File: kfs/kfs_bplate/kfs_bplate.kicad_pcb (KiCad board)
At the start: 2 copper layers, 256 x 90.6 mm, 10 parts

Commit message: Slight mods to kfs.
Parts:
- added H1: MountingHole, MountingHole:MountingHole_4mm, F.Cu at (135.0, 34.0)
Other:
- board size 256 x 90.6 mm -> 256 x 94.5 mm
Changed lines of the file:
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@@
     (pad "1" thru_hole circle (at 0 0) (size 3.5 3.5) (drill 2.2) (layers "*.Cu" "*.Mask"))
+  )
+  (footprint "MountingHole:MountingHole_4mm" (layer "F.Cu")
+    (at 135 34)
+    (descr "Mounting Hole 4mm, no annular")
+    (tags "mounting hole 4mm no annular")
+    (property "Sheetfile" "kfs_bplate.kicad_sch")
+    (property "Sheetname" "")
+    (property "ki_description" "Mounting Hole without connection")
+    (property "ki_keywords" "mounting hole")
+    (attr exclude_from_pos_files)
+    (fp_text reference "H1" (at 0 -5) (layer "F.SilkS") hide
+        (effects (font (size 1 1) (thickness 0.15)))
+    )
+    (fp_text value "MountingHole" (at 0 5) (layer "F.Fab")
+        (effects (font (size 1 1) (thickness 0.15)))
+    )
+    (fp_text user "${REFERENCE}" (at 0 0) (layer "F.Fab")
+        (effects (font (size 1 1) (thickness 0.15)))
+    )
+    (fp_circle (center 0 0) (end 4 0)
+      (stroke (width 0.15) (type solid)) (fill none) (layer "Cmts.User"))
+    (fp_circle (center 0 0) (end 4.25 0)
+      (stroke (width 0.05) (type solid)) (fill none) (layer "F.CrtYd"))
+    (pad "" np_thru_hole circle (at 0 0) (size 4 4) (drill 4) (layers "*.Cu" "*.Mask"))
   )
   (footprint "MountingHole:MountingHole_2.2mm_M2_ISO7380_Pad" (layer "F.Cu")
@@
     (pad "1" thru_hole circle (at 0 0) (size 3.5 3.5) (drill 2.2) (layers "*.Cu" "*.Mask"))
   )
-  (gr_line (start 268 21.94) (end 20 21.94)
+  (gr_line (start 268 18) (end 20 18)
     (stroke (width 0.1) (type default)) (layer "Edge.Cuts"))
-  (gr_arc (start 16 25.94) (mid 17.171573 23.111573) (end 20 21.94)
+  (gr_arc (start 16 22) (mid 17.171573 19.171573) (end 20 18)
     (stroke (width 0.1) (type default)) (layer "Edge.Cuts"))
   (gr_arc (start 20 112.5) (mid 17.171573 111.328427) (end 16 108.5)
     (stroke (width 0.1) (type default)) (layer "Edge.Cuts"))
-  (gr_arc (start 268 21.94) (mid 270.828427 23.111573) (end 272 25.94)
-    (stroke (width 0.1) (type default)) (layer "Edge.Cuts"))
   (gr_arc (start 272 108.5) (mid 270.828427 111.328427) (end 268 112.5)
     (stroke (width 0.1) (type default)) (layer "Edge.Cuts"))
-  (gr_line (start 16 25.94) (end 16 108.5)
+  (gr_line (start 16 22) (end 16 108.5)
     (stroke (width 0.1) (type default)) (layer "Edge.Cuts"))
   (gr_line (start 20 112.5) (end 268 112.5)
     (stroke (width 0.1) (type default)) (layer "Edge.Cuts"))
-  (gr_line (start 272 108.5) (end 272 25.94)
+  (gr_line (start 272 108.5) (end 272 22)
+    (stroke (width 0.1) (type default)) (layer "Edge.Cuts"))
+  (gr_arc (start 268 18) (mid 270.828427 19.171573) (end 272 22)
     (stroke (width 0.1) (type default)) (layer "Edge.Cuts"))
 )

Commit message: Moved some mounting holes on the kfs.
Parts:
- moved H0 23.2 mm to (148.0, 24.0)
- moved H4 23.2 mm to (122.0, 24.0)
- moved H3 17.0 mm to (216.0, 59.5)
- moved H7 14.1 mm to (22.0, 24.0)
- moved H9 14.1 mm to (266.0, 24.0)
- moved H10 4.53 mm to (266.0, 106.5)
- moved H8 4.53 mm to (22.0, 106.5)
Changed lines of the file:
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@@
   (net 0 "")
   (footprint "MountingHole:MountingHole_2.2mm_M2_ISO7380_Pad" (layer "F.Cu")
-    (at 162 42.5)
+    (at 148 24)
     (descr "Mounting Hole 2.2mm, M2, ISO7380")
     (tags "mounting hole 2.2mm m2 iso7380")
@@
   )
   (footprint "MountingHole:MountingHole_2.2mm_M2_ISO7380_Pad" (layer "F.Cu")
-    (at 265.5 102)
+    (at 266 106.5)
     (descr "Mounting Hole 2.2mm, M2, ISO7380")
     (tags "mounting hole 2.2mm m2 iso7380")
@@
   )
   (footprint "MountingHole:MountingHole_2.2mm_M2_ISO7380_Pad" (layer "F.Cu")
-    (at 22.5 102)
+    (at 22 106.5)
     (descr "Mounting Hole 2.2mm, M2, ISO7380")
     (tags "mounting hole 2.2mm m2 iso7380")
@@
   )
   (footprint "MountingHole:MountingHole_2.2mm_M2_ISO7380_Pad" (layer "F.Cu")
-    (at 36 25.5)
+    (at 22 24)
     (descr "Mounting Hole 2.2mm, M2, ISO7380")
     (tags "mounting hole 2.2mm m2 iso7380")
@@
   )
   (footprint "MountingHole:MountingHole_2.2mm_M2_ISO7380_Pad" (layer "F.Cu")
-    (at 108 42.5)
+    (at 122 24)
     (descr "Mounting Hole 2.2mm, M2, ISO7380")
     (tags "mounting hole 2.2mm m2 iso7380")
@@
   )
   (footprint "MountingHole:MountingHole_2.2mm_M2_ISO7380_Pad" (layer "F.Cu")
-    (at 216 76.5)
+    (at 216 59.5)
     (descr "Mounting Hole 2.2mm, M2, ISO7380")
     (tags "mounting hole 2.2mm m2 iso7380")
@@
   )
   (footprint "MountingHole:MountingHole_2.2mm_M2_ISO7380_Pad" (layer "F.Cu")
-    (at 252 25.5)
-    (descr "Mounting Hole 2.2mm, M2, ISO7380")
-    (tags "mounting hole 2.2mm m2 iso7380")
+    (at 266 24)
+    (descr "Mounting Hole 2.2mm, M2, ISO7380")
+    (tags "mounting hole 2.2mm m2 iso7380")

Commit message: Switched to staggered kfs layout.
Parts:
- H1: footprint MountingHole:MountingHole_4mm -> MountingHole:MountingHole_8.4mm_M8
- moved H3 200.3 mm to (16.5, 41.5)
- moved H8 196.2 mm to (216.0, 77.0)
- moved H5 184.1 mm to (289.5, 124.5)
- moved H10 150.7 mm to (130.0, 41.5)
- moved H2 137.7 mm to (289.5, 41.5)
- moved H4 114.1 mm to (176.0, 124.5)
- moved H9 109.4 mm to (158.0, 41.5)
- moved H0 106.8 mm to (112.0, 124.5)
- moved H6 85.5 mm to (16.5, 124.5)
- moved H7 72.9 mm to (72.0, 77.0)
- moved H1 19.2 mm to (144.0, 51.0)
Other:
- board size 256 x 94.5 mm -> 283 x 93 mm
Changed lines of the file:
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@@
   (net 0 "")
   (footprint "MountingHole:MountingHole_2.2mm_M2_ISO7380_Pad" (layer "F.Cu")
-    (at 148 24)
+    (at 112 124.5)
     (descr "Mounting Hole 2.2mm, M2, ISO7380")
     (tags "mounting hole 2.2mm m2 iso7380")
@@
   )
   (footprint "MountingHole:MountingHole_2.2mm_M2_ISO7380_Pad" (layer "F.Cu")
-    (at 266 106.5)
+    (at 130 41.5)
     (descr "Mounting Hole 2.2mm, M2, ISO7380")
     (tags "mounting hole 2.2mm m2 iso7380")
@@
   )
   (footprint "MountingHole:MountingHole_2.2mm_M2_ISO7380_Pad" (layer "F.Cu")
-    (at 162 93.5)
+    (at 289.5 41.5)
     (descr "Mounting Hole 2.2mm, M2, ISO7380")
     (tags "mounting hole 2.2mm m2 iso7380")
@@
     (pad "1" thru_hole circle (at 0 0) (size 3.5 3.5) (drill 2.2) (layers "*.Cu" "*.Mask"))
   )
-  (footprint "MountingHole:MountingHole_2.2mm_M2_ISO7380_Pad" (layer "F.Cu")
-    (at 72 59.5)
+  (footprint "MountingHole:MountingHole_8.4mm_M8" (layer "F.Cu")
+    (at 144 51)
+    (descr "Mounting Hole 8.4mm, no annular, M8")
+    (tags "mounting hole 8.4mm no annular m8")
+    (property "Sheetfile" "kfs_bplate.kicad_sch")
+    (property "Sheetname" "")
+    (property "ki_description" "Mounting Hole without connection")
+    (property "ki_keywords" "mounting hole")
+    (attr exclude_from_pos_files)
+    (fp_text reference "H1" (at 0 -9.4) (layer "F.SilkS") hide
+        (effects (font (size 1 1) (thickness 0.15)))
+    )
+    (fp_text value "MountingHole" (at 0 9.4) (layer "F.Fab")
+        (effects (font (size 1 1) (thickness 0.15)))
+    )
+    (fp_text user "${REFERENCE}" (at 0 0) (layer "F.Fab")
+        (effects (font (size 1 1) (thickness 0.15)))
+    )
+    (fp_circle (center 0 0) (end 8.4 0)
+      (stroke (width 0.15) (type solid)) (fill none) (layer "Cmts.User"))
+    (fp_circle (center 0 0) (end 8.65 0)
+      (stroke (width 0.05) (type solid)) (fill none) (layer "F.CrtYd"))
+    (pad "" np_thru_hole circle (at 0 0) (size 8.4 8.4) (drill 8.4) (layers "*.Cu" "*.Mask"))
+  )
+  (footprint "MountingHole:MountingHole_2.2mm_M2_ISO7380_Pad" (layer "F.Cu")
+    (at 16.5 124.5)
     (descr "Mounting Hole 2.2mm, M2, ISO7380")
     (tags "mounting hole 2.2mm m2 iso7380")
@@
   )
   (footprint "MountingHole:MountingHole_2.2mm_M2_ISO7380_Pad" (layer "F.Cu")
-    (at 22 106.5)
+    (at 216 77)
     (descr "Mounting Hole 2.2mm, M2, ISO7380")
     (tags "mounting hole 2.2mm m2 iso7380")
@@
   )
   (footprint "MountingHole:MountingHole_2.2mm_M2_ISO7380_Pad" (layer "F.Cu")
-    (at 22 24)
+    (at 72 77)
     (descr "Mounting Hole 2.2mm, M2, ISO7380")
     (tags "mounting hole 2.2mm m2 iso7380")
@@
   )
   (footprint "MountingHole:MountingHole_2.2mm_M2_ISO7380_Pad" (layer "F.Cu")
-    (at 122 24)
+    (at 176 124.5)
     (descr "Mounting Hole 2.2mm, M2, ISO7380")
     (tags "mounting hole 2.2mm m2 iso7380")
@@
   )
   (footprint "MountingHole:MountingHole_2.2mm_M2_ISO7380_Pad" (layer "F.Cu")
-    (at 108 93.5)
+    (at 289.5 124.5)
     (descr "Mounting Hole 2.2mm, M2, ISO7380")
     (tags "mounting hole 2.2mm m2 iso7380")
@@
   )
   (footprint "MountingHole:MountingHole_2.2mm_M2_ISO7380_Pad" (layer "F.Cu")
-    (at 216 59.5)
+    (at 16.5 41.5)
     (descr "Mounting Hole 2.2mm, M2, ISO7380")
     (tags "mounting hole 2.2mm m2 iso7380")
@@
     (pad "1" thru_hole circle (at 0 0) (size 3.5 3.5) (drill 2.2) (layers "*.Cu" "*.Mask"))
   )
-  (footprint "MountingHole:MountingHole_4mm" (layer "F.Cu")
-    (at 135 34)
-    (descr "Mounting Hole 4mm, no annular")
-    (tags "mounting hole 4mm no annular")
-    (property "Sheetfile" "kfs_bplate.kicad_sch")
-    (property "Sheetname" "")
-    (property "ki_description" "Mounting Hole without connection")
-    (property "ki_keywords" "mounting hole")
-    (attr exclude_from_pos_files)
-    (fp_text reference "H1" (at 0 -5) (layer "F.SilkS") hide
-        (effects (font (size 1 1) (thickness 0.15)))
-    )
-    (fp_text value "MountingHole" (at 0 5) (layer "F.Fab")
-        (effects (font (size 1 1) (thickness 0.15)))
-    )
-    (fp_text user "${REFERENCE}" (at 0 0) (layer "F.Fab")
-        (effects (font (size 1 1) (thickness 0.15)))
-    )
-    (fp_circle (center 0 0) (end 4 0)
-      (stroke (width 0.15) (type solid)) (fill none) (layer "Cmts.User"))
-    (fp_circle (center 0 0) (end 4.25 0)
-      (stroke (width 0.05) (type solid)) (fill none) (layer "F.CrtYd"))
-    (pad "" np_thru_hole circle (at 0 0) (size 4 4) (drill 4) (layers "*.Cu" "*.Mask"))
-  )
-  (footprint "MountingHole:MountingHole_2.2mm_M2_ISO7380_Pad" (layer "F.Cu")
-    (at 266 24)
+  (footprint "MountingHole:MountingHole_2.2mm_M2_ISO7380_Pad" (layer "F.Cu")
+    (at 158 41.5)
     (descr "Mounting Hole 2.2mm, M2, ISO7380")
     (tags "mounting hole 2.2mm m2 iso7380")
@@
     (pad "1" thru_hole circle (at 0 0) (size 3.5 3.5) (drill 2.2) (layers "*.Cu" "*.Mask"))
   )
-  (gr_line (start 268 18) (end 20 18)
-    (stroke (width 0.1) (type default)) (layer "Edge.Cuts"))
-  (gr_arc (start 16 22) (mid 17.171573 19.171573) (end 20 18)
-    (stroke (width 0.1) (type default)) (layer "Edge.Cuts"))
-  (gr_arc (start 20 112.5) (mid 17.171573 111.328427) (end 16 108.5)
-    (stroke (width 0.1) (type default)) (layer "Edge.Cuts"))
-  (gr_arc (start 272 108.5) (mid 270.828427 111.328427) (end 268 112.5)
-    (stroke (width 0.1) (type default)) (layer "Edge.Cuts"))
-  (gr_line (start 16 22) (end 16 108.5)
-    (stroke (width 0.1) (type default)) (layer "Edge.Cuts"))
-  (gr_line (start 20 112.5) (end 268 112.5)
-    (stroke (width 0.1) (type default)) (layer "Edge.Cuts"))
-  (gr_line (start 272 108.5) (end 272 22)
-    (stroke (width 0.1) (type default)) (layer "Edge.Cuts"))
-  (gr_arc (start 268 18) (mid 270.828427 19.171573) (end 272 22)
+  (gr_arc (start 16.5 129.5) (mid 12.964466 128.035534) (end 11.5 124.5)
+    (stroke (width 0.1) (type default)) (layer "Edge.Cuts"))
+  (gr_arc (start 11.5 41.5) (mid 12.964466 37.964466) (end 16.5 36.5)
+    (stroke (width 0.1) (type default)) (layer "Edge.Cuts"))
+  (gr_line (start 16.5 36.5) (end 289.5 36.5)
+    (stroke (width 0.1) (type default)) (layer "Edge.Cuts"))
+  (gr_line (start 11.5 124.5) (end 11.5 41.5)
+    (stroke (width 0.1) (type default)) (layer "Edge.Cuts"))
+  (gr_line (start 294.5 41.5) (end 294.5 124.5)
+    (stroke (width 0.1) (type default)) (layer "Edge.Cuts"))
+  (gr_arc (start 289.5 36.5) (mid 293.035534 37.964466) (end 294.5 41.5)
+    (stroke (width 0.1) (type default)) (layer "Edge.Cuts"))
+  (gr_arc (start 294.5 124.5) (mid 293.035534 128.035534) (end 289.5 129.5)
+    (stroke (width 0.1) (type default)) (layer "Edge.Cuts"))
+  (gr_line (start 289.5 129.5) (end 16.5 129.5)
     (stroke (width 0.1) (type default)) (layer "Edge.Cuts"))
 )

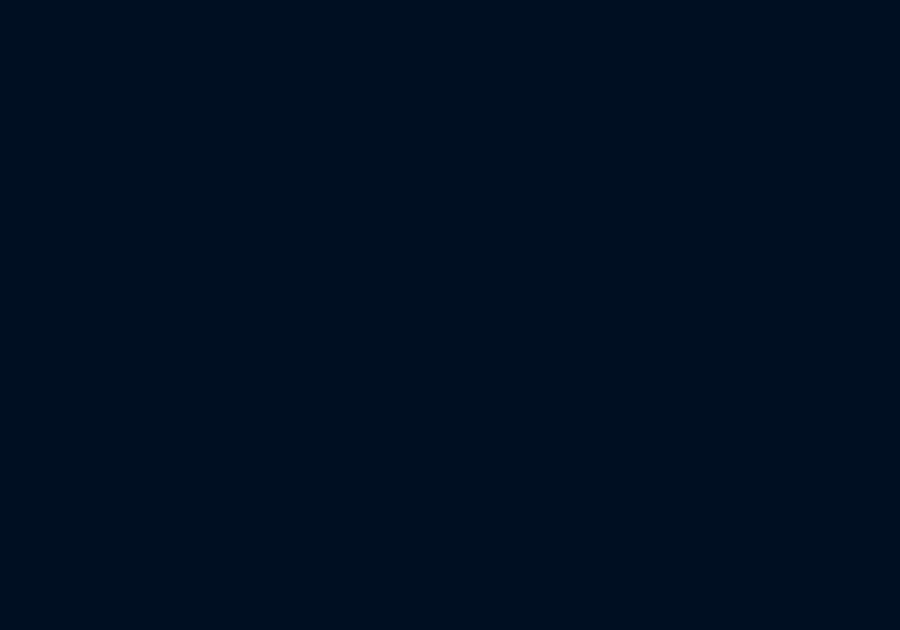
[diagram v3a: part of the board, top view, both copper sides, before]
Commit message: Moved the bottom row of kfs farther inward.
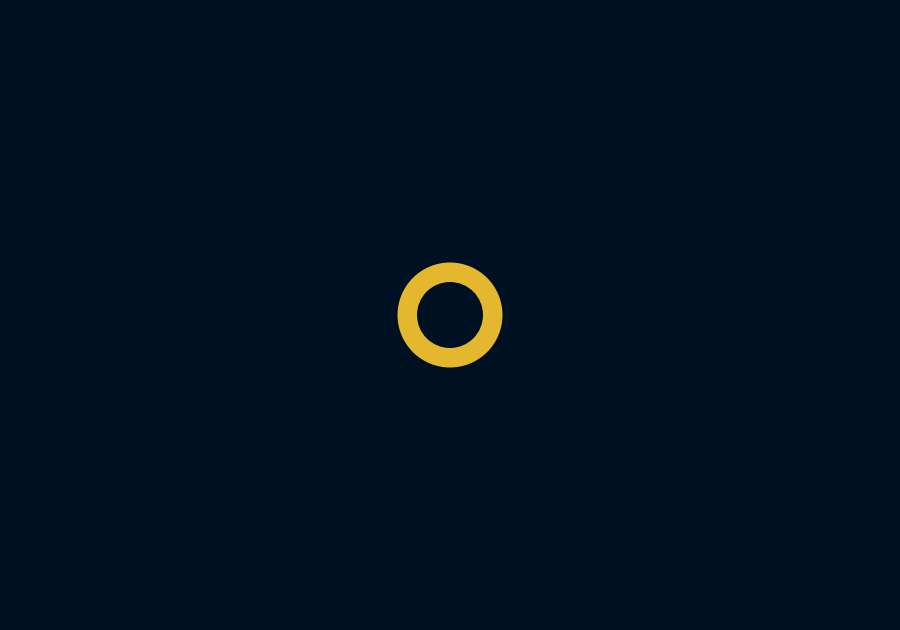
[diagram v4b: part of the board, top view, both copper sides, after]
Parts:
- added H11: MountingHole, MountingHole:MountingHole_2.2mm_M2_ISO7380_Pad, F.Cu at (153.0, 93.5)
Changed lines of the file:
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@@
+  )
+  (footprint "MountingHole:MountingHole_2.2mm_M2_ISO7380_Pad" (layer "F.Cu")
+    (at 153 93.5)
+    (descr "Mounting Hole 2.2mm, M2, ISO7380")
+    (tags "mounting hole 2.2mm m2 iso7380")
+    (property "Sheetfile" "kfs_bplate.kicad_sch")
+    (property "Sheetname" "")
+    (property "ki_description" "Mounting Hole without connection")
+    (property "ki_keywords" "mounting hole")
+    (attr exclude_from_pos_files)
+    (fp_text reference "H11" (at 0 -2.75) (layer "F.SilkS") hide
+        (effects (font (size 1 1) (thickness 0.15)))
+    )
+    (fp_text value "MountingHole" (at 0 2.75) (layer "F.Fab")
+        (effects (font (size 1 1) (thickness 0.15)))
+    )
+    (fp_text user "${REFERENCE}" (at 0 0) (layer "F.Fab")
+        (effects (font (size 1 1) (thickness 0.15)))
+    )
+    (fp_circle (center 0 0) (end 1.75 0)
+      (stroke (width 0.15) (type solid)) (fill none) (layer "Cmts.User"))
+    (fp_circle (center 0 0) (end 2 0)
+      (stroke (width 0.05) (type solid)) (fill none) (layer "F.CrtYd"))
+    (pad "1" thru_hole circle (at 0 0) (size 3.5 3.5) (drill 2.2) (layers "*.Cu" "*.Mask"))
   )
   (footprint "MountingHole:MountingHole_2.2mm_M2_ISO7380_Pad" (layer "F.Cu")

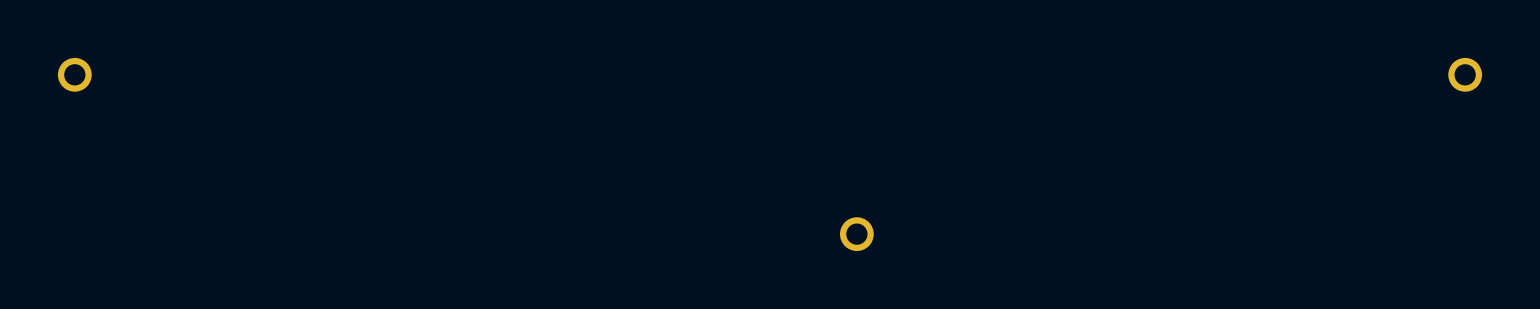
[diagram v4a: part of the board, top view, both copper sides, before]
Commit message: Updated reset button and mounting holes on kfs.
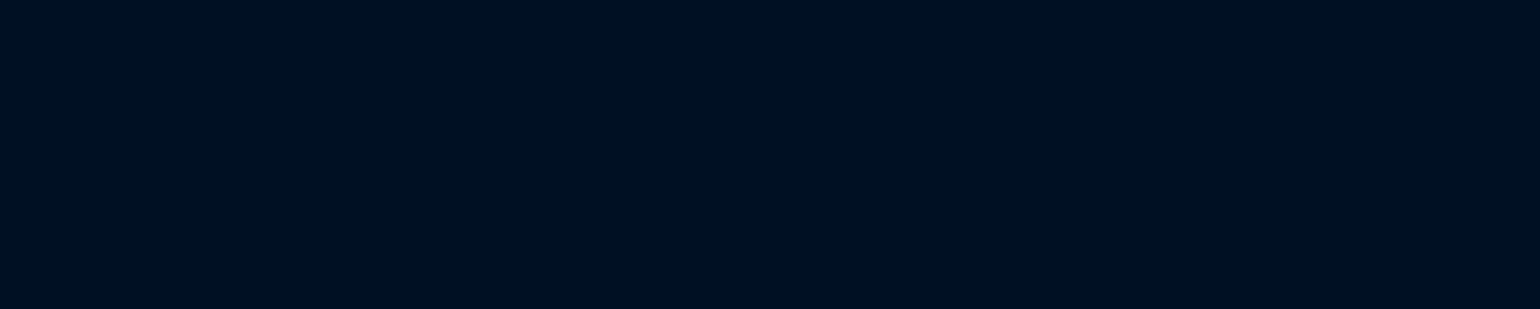
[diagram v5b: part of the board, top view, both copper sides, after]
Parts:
- removed H11, H7, H8: MountingHole, MountingHole:MountingHole_2.2mm_M2_ISO7380_Pad
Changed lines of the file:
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@@
-  )
-  (footprint "MountingHole:MountingHole_2.2mm_M2_ISO7380_Pad" (layer "F.Cu")
-    (at 153 93.5)
-    (descr "Mounting Hole 2.2mm, M2, ISO7380")
-    (tags "mounting hole 2.2mm m2 iso7380")
-    (property "Sheetfile" "kfs_bplate.kicad_sch")
-    (property "Sheetname" "")
-    (property "ki_description" "Mounting Hole without connection")
-    (property "ki_keywords" "mounting hole")
-    (attr exclude_from_pos_files)
-    (fp_text reference "H11" (at 0 -2.75) (layer "F.SilkS") hide
-        (effects (font (size 1 1) (thickness 0.15)))
-    )
-    (fp_text value "MountingHole" (at 0 2.75) (layer "F.Fab")
-        (effects (font (size 1 1) (thickness 0.15)))
-    )
-    (fp_text user "${REFERENCE}" (at 0 0) (layer "F.Fab")
-        (effects (font (size 1 1) (thickness 0.15)))
-    )
-    (fp_circle (center 0 0) (end 1.75 0)
-      (stroke (width 0.15) (type solid)) (fill none) (layer "Cmts.User"))
-    (fp_circle (center 0 0) (end 2 0)
-      (stroke (width 0.05) (type solid)) (fill none) (layer "F.CrtYd"))
-    (pad "1" thru_hole circle (at 0 0) (size 3.5 3.5) (drill 2.2) (layers "*.Cu" "*.Mask"))
   )
   (footprint "MountingHole:MountingHole_2.2mm_M2_ISO7380_Pad" (layer "F.Cu")
@@
         (effects (font (size 1 1) (thickness 0.15)))
     )
-    (fp_text value "MountingHole" (at 0 2.75) (layer "F.Fab")
-        (effects (font (size 1 1) (thickness 0.15)))
-    )
-    (fp_text user "${REFERENCE}" (at 0 0) (layer "F.Fab")
-        (effects (font (size 1 1) (thickness 0.15)))
-    )
-    (fp_circle (center 0 0) (end 1.75 0)
-      (stroke (width 0.15) (type solid)) (fill none) (layer "Cmts.User"))
-    (fp_circle (center 0 0) (end 2 0)
-      (stroke (width 0.05) (type solid)) (fill none) (layer "F.CrtYd"))
-    (pad "1" thru_hole circle (at 0 0) (size 3.5 3.5) (drill 2.2) (layers "*.Cu" "*.Mask"))
-  )
-  (footprint "MountingHole:MountingHole_2.2mm_M2_ISO7380_Pad" (layer "F.Cu")
-    (at 216 77)
-    (descr "Mounting Hole 2.2mm, M2, ISO7380")
-    (tags "mounting hole 2.2mm m2 iso7380")
-    (property "Sheetfile" "kfs_bplate.kicad_sch")
-    (property "Sheetname" "")
-    (property "ki_description" "Mounting Hole without connection")
-    (property "ki_keywords" "mounting hole")
-    (attr exclude_from_pos_files)
-    (fp_text reference "H8" (at 0 -2.75) (layer "F.SilkS") hide
-        (effects (font (size 1 1) (thickness 0.15)))
-    )
-    (fp_text value "MountingHole" (at 0 2.75) (layer "F.Fab")
-        (effects (font (size 1 1) (thickness 0.15)))
-    )
-    (fp_text user "${REFERENCE}" (at 0 0) (layer "F.Fab")
-        (effects (font (size 1 1) (thickness 0.15)))
-    )
-    (fp_circle (center 0 0) (end 1.75 0)
-      (stroke (width 0.15) (type solid)) (fill none) (layer "Cmts.User"))
-    (fp_circle (center 0 0) (end 2 0)
-      (stroke (width 0.05) (type solid)) (fill none) (layer "F.CrtYd"))
-    (pad "1" thru_hole circle (at 0 0) (size 3.5 3.5) (drill 2.2) (layers "*.Cu" "*.Mask"))
-  )
-  (footprint "MountingHole:MountingHole_2.2mm_M2_ISO7380_Pad" (layer "F.Cu")
-    (at 72 77)
-    (descr "Mounting Hole 2.2mm, M2, ISO7380")
-    (tags "mounting hole 2.2mm m2 iso7380")
-    (property "Sheetfile" "kfs_bplate.kicad_sch")
-    (property "Sheetname" "")
-    (property "ki_description" "Mounting Hole without connection")
-    (property "ki_keywords" "mounting hole")
-    (attr exclude_from_pos_files)
-    (fp_text reference "H7" (at 0 -2.75) (layer "F.SilkS") hide
-        (effects (font (size 1 1) (thickness 0.15)))
-    )
